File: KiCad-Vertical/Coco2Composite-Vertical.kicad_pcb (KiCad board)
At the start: 2 copper layers, 65.1 x 39.7 mm, 17 parts, among them J1 TO_COCO2, J2 AUDIO_JACK_3.5MM_KIT, Q1 PN2907, Q2 2N2222, U1 MC1372

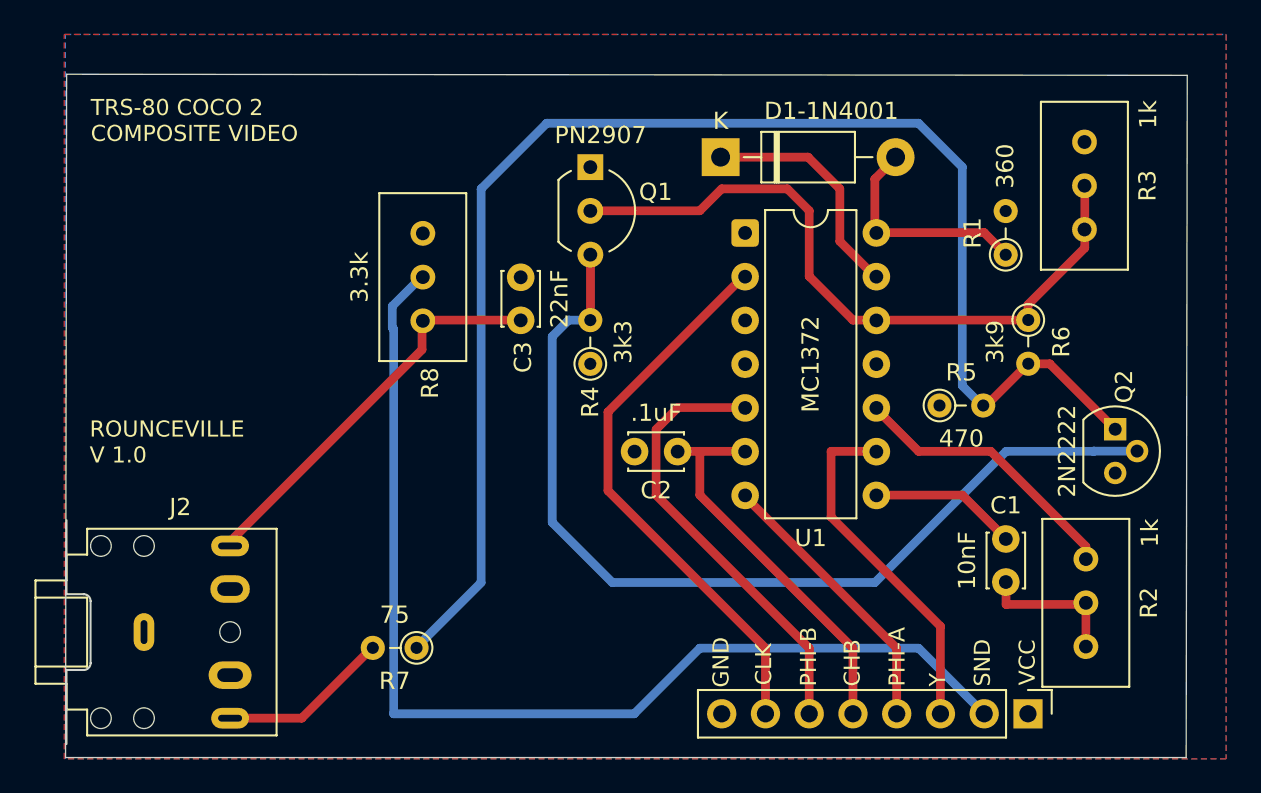
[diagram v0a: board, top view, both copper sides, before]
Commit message: Updated the vertical model to let the resistors lie down on the board, kept the old one in case someone wants the board the same way it was
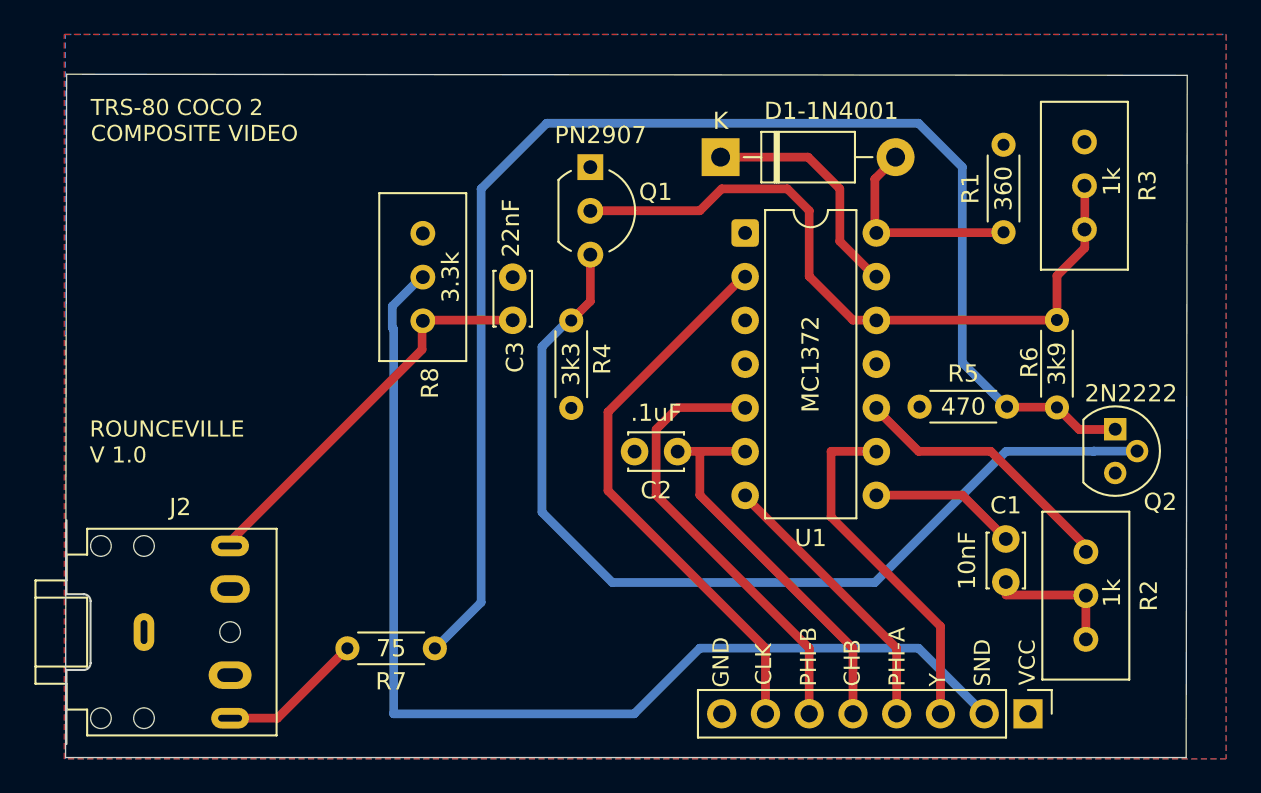
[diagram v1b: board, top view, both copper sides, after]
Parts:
- R1, R4, R5, R6, R7: footprint Resistor_THT:R_Axial_DIN0204_L3.6mm_D1.6mm_P2.54mm_Vertical -> Resistor_THT:R_Axial_DIN0204_L3.6mm_D1.6mm_P5.08mm_Horizontal
- moved R4 2.79 mm to (145.3, 104.5)
- moved R6 1.67 mm to (173.5, 99.4)
- moved R1 1.31 mm to (170.4, 94.3)
- moved R5 1.16 mm to (165.5, 104.5)
- moved R7 1.06 mm to (137.4, 118.5)
- moved C3 0.46 mm to (141.9, 99.5)
- moved R2 0.42 mm to (175.2, 118.0)
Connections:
- D1-1N4001 pad 1: (no net) -> Net-(U1-RF_TANK_1)
- D1-1N4001 pad 2: (no net) -> Net-(U1-RF_TANK_2)
- J2 pad R: (no net) -> Net-(C3-Pad1)
- J2 pad T: (no net) -> Net-(J2-PadTIP)
- R2 pad 1: (no net) -> Net-(C1-Pad2)
- R2 pad 2: (no net) -> Net-(C1-Pad2)
- R2 pad 3: (no net) -> Net-(U1-CHROM_IN)
- R3 pad 1: (no net) -> Net-(U1-RF_OUT)
- R3 pad 2: (no net) -> Net-(U1-RF_OUT)
- R8 pad 1: (no net) -> Net-(C3-Pad1)
- R8 pad 2: (no net) -> Net-(J1-Pad2)
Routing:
- net Net-(Q2-E): track 83.6 -> 80.1 mm
- net Net-(J2-PadTIP): track 9.56 -> 8.15 mm
- net Net-(U1-RF_OUT): track 40.4 -> 41.4 mm
- net Net-(U1-RF_TANK_2): track 13.1 -> 12.4 mm
- net Net-(U1-CHROM_IN): track 16.4 -> 15.9 mm
- net Net-(C1-Pad2): track 8.45 -> 7.93 mm

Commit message: Increased the footprint for the resistors since the one I picked was still too small
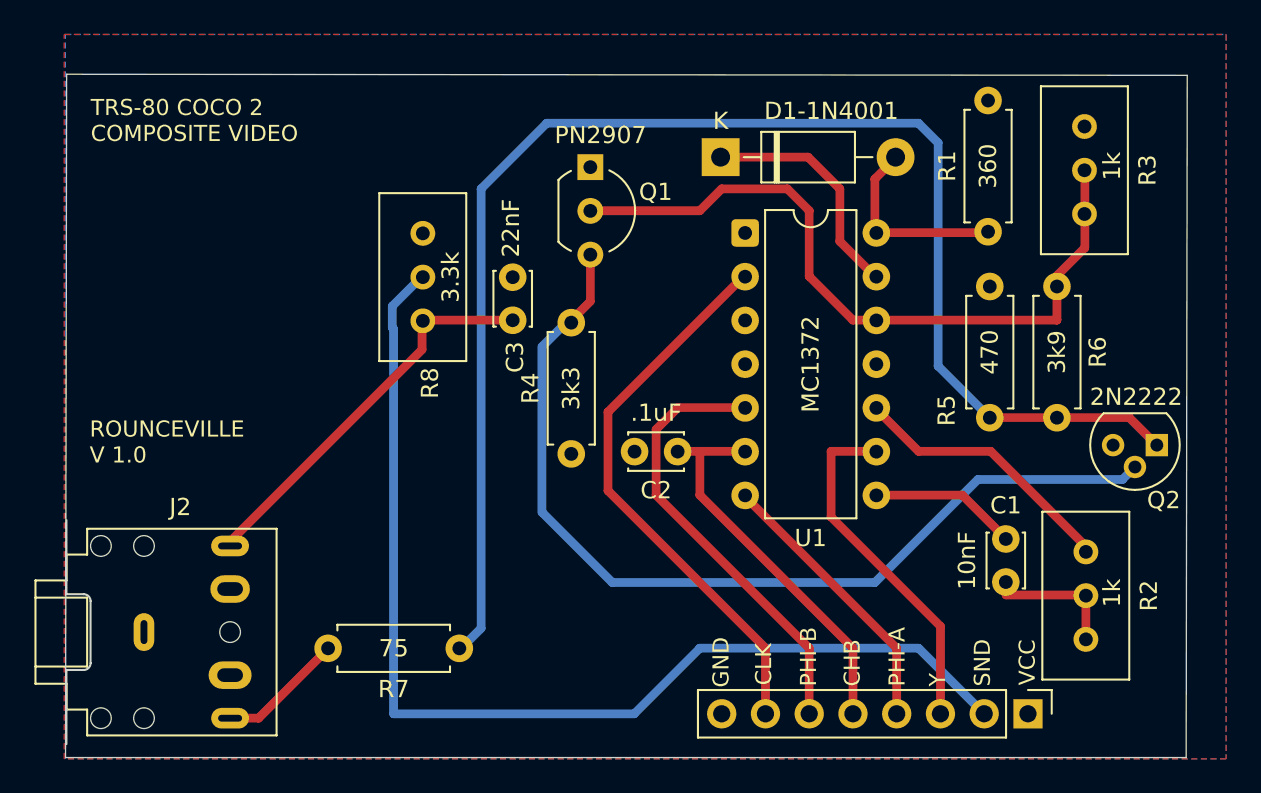
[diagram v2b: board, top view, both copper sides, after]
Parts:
- R1, R4, R5, R6, R7: footprint Resistor_THT:R_Axial_DIN0204_L3.6mm_D1.6mm_P5.08mm_Horizontal -> Resistor_THT:R_Axial_DIN0207_L6.3mm_D2.5mm_P7.62mm_Horizontal
- moved R5 8.08 mm to (169.6, 97.5), turned to -90 degrees
- moved R4 2.67 mm to (145.3, 107.2)
- moved Q2 2.59 mm to (179.3, 106.7), turned to 180 degrees
- moved R6 1.94 mm to (173.5, 97.5)
- moved R7 1.42 mm to (138.8, 118.5)
- moved R1 0.90 mm to (169.5, 94.3)
- moved R3 0.90 mm to (175.1, 93.3)
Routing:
- net Net-(Q2-E): track 80.1 -> 83.4 mm
- net Net-(J2-PadTIP): track 8.15 -> 7.03 mm
- net Net-(U1-RF_OUT): track 41.4 -> 42.4 mm
- net Net-(U1-RF_TANK_2): track 12.4 -> 11.5 mm
- net Net-(Q2-B): track 55.5 -> 55.0 mm

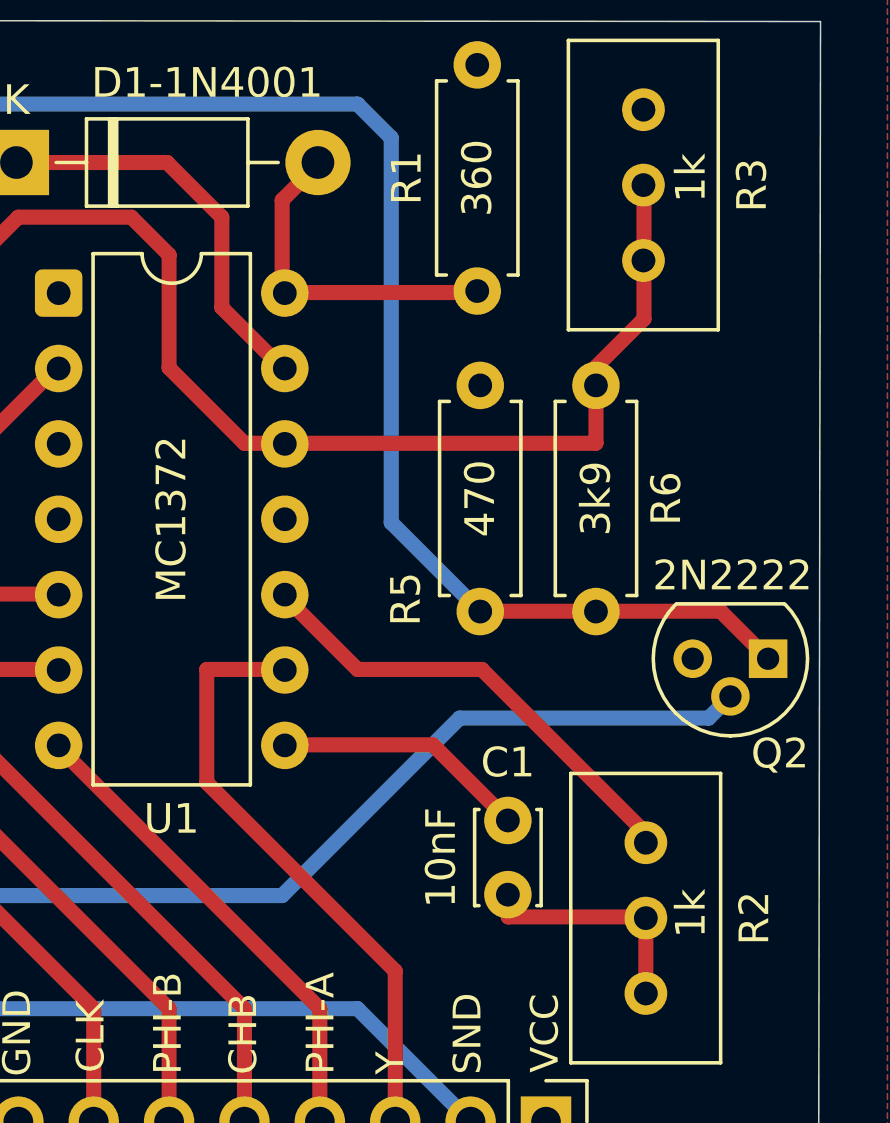
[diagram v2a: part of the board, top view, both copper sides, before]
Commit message: minor updates to the vertical PCB to clean up trace paths
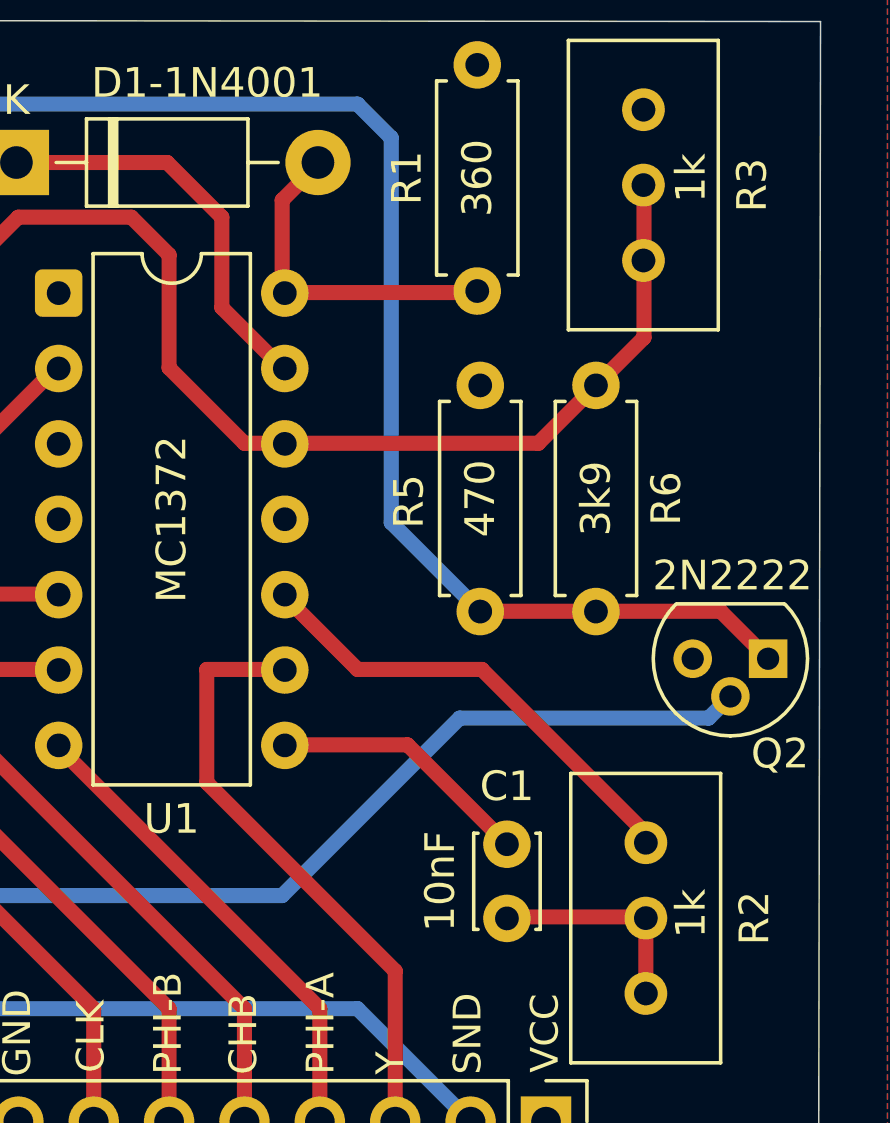
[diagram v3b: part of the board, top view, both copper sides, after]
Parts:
- moved C1 0.80 mm to (170.5, 113.0)
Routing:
- net Net-(U1-RF_OUT): track 42.4 -> 41.2 mm
- net Net-(C1-Pad2): track 7.93 -> 7.28 mm
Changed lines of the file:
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@@
 		(tags "Resistor Axial_DIN0207 series Axial Horizontal pin pitch 7.62mm 0.25W = 1/4W length 6.3mm diameter 2.5mm")
 		(property "Reference" "R5"
-			(at 7.2 2.5 90)
+			(at 3.91 2.4 90)
 			(layer "F.SilkS")
 			(effects
@@
 	(footprint "Capacitor_THT:C_Disc_D3.0mm_W2.0mm_P2.50mm"
 		(layer "F.Cu")
-		(at 170.531478 112.15 -90)
+		(at 170.5 112.95 -90)
 		(descr "C, Disc series, Radial, pin pitch=2.50mm, diameter*width=3*2mm^2, Capacitor")
 		(tags "C Disc series Radial pin pitch 2.50mm diameter 3mm width 2mm Capacitor")
@@
 	(segment
 		(start 175.1811 115.4)
-		(end 170.5456 115.4)
+		(end 170.55 115.4)
 		(width 0.508)
 		(layer "F.Cu")
@@
 	)
 	(segment
-		(start 170.5456 115.4)
-		(end 170.5456 114.6811)
+		(start 170.55 115.4)
+		(end 170.5 115.45)
 		(width 0.508)
 		(layer "F.Cu")
@@
 	)
 	(segment
-		(start 168.0056 109.6011)
-		(end 162.9256 109.6011)
+		(start 170.5 112.95)
+		(end 167.1511 109.6011)
 		(width 0.508)
 		(layer "F.Cu")
@@
 	)
 	(segment
-		(start 170.5456 112.1411)
-		(end 168.0056 109.6011)
+		(start 167.1511 109.6011)
+		(end 162.9256 109.6011)
 		(width 0.508)
 		(layer "F.Cu")
@@
 	)
 	(segment
-		(start 173.5 99.434179)
-		(end 173.493079 99.4411)
-		(width 0.508)
-		(layer "F.Cu")
-		(net 15)
-	)
-	(segment
 		(start 161.6556 99.4411)
 		(end 159.1156 96.9011)
@@
 	)
 	(segment
-		(start 175.1176 95.2501)
-		(end 173.5 96.8677)
-		(width 0.508)
-		(layer "F.Cu")
-		(net 15)
-	)
-	(segment
-		(start 175.1 90.74)
-		(end 175.1176 90.7576)
+		(start 171.5589 99.4411)
+		(end 161.6556 99.4411)
 		(width 0.508)
 		(layer "F.Cu")
@@
 	)
 	(segment
-		(start 173.5 96.8677)
-		(end 173.5 99.434179)
+		(start 154.0356 91.8211)
+		(end 152.7656 93.0911)
 		(width 0.508)
 		(layer "F.Cu")
@@
 	(segment
 		(start 175.1176 90.7576)
-		(end 175.1176 95.2501)
+		(end 175.1176 95.8824)
 		(width 0.508)
 		(layer "F.Cu")
@@
 	)
 	(segment
-		(start 173.493079 99.4411)
-		(end 161.6556 99.4411)
+		(start 159.1156 96.9011)
+		(end 159.1156 93.0911)
 		(width 0.508)
 		(layer "F.Cu")
@@
 	)
 	(segment
-		(start 154.0356 91.8211)
-		(end 152.7656 93.0911)
+		(start 157.8456 91.8211)
+		(end 154.0356 91.8211)
 		(width 0.508)
 		(layer "F.Cu")
@@
 	)
 	(segment
-		(start 157.8456 91.8211)
-		(end 154.0356 91.8211)
+		(start 175.1 90.74)
+		(end 175.1176 90.7576)
 		(width 0.508)
 		(layer "F.Cu")
@@
 	)
 	(segment
-		(start 152.7656 93.0911)
-		(end 146.4156 93.0911)
+		(start 175.1176 95.8824)
+		(end 171.5589 99.4411)
 		(width 0.508)
 		(layer "F.Cu")
@@
 	)
 	(segment
-		(start 159.1156 96.9011)
-		(end 159.1156 93.0911)
+		(start 159.1156 93.0911)
+		(end 157.8456 91.8211)
 		(width 0.508)
 		(layer "F.Cu")
@@
 	)
 	(segment
-		(start 159.1156 93.0911)
-		(end 157.8456 91.8211)
+		(start 152.7656 93.0911)
+		(end 146.4156 93.0911)
 		(width 0.508)
 		(layer "F.Cu")
